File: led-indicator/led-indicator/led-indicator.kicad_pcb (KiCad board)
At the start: 2 copper layers, 49.9 x 35.7 mm, 36 parts, among them CN1 XT30U-M, J2 JST_XH_3pin, U1 74AHCT125

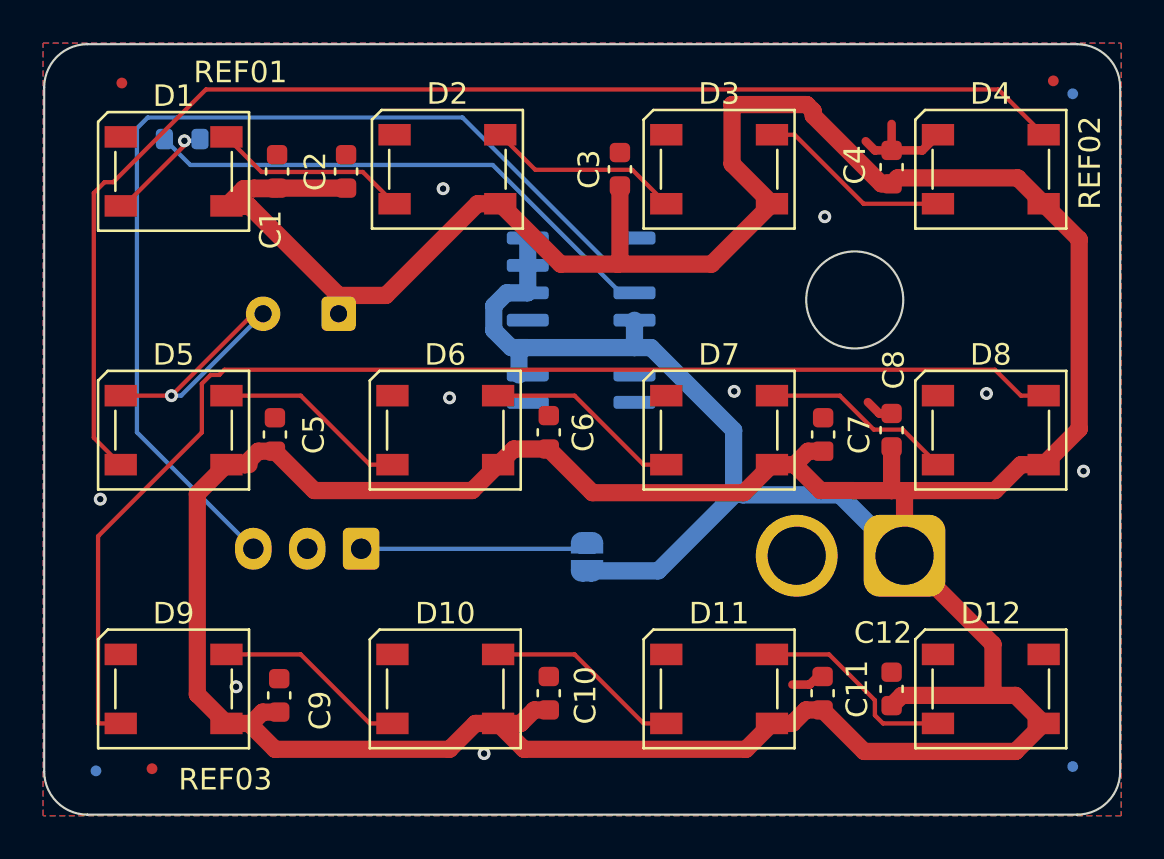
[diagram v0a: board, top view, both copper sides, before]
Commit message: Updated to be single-sided board.
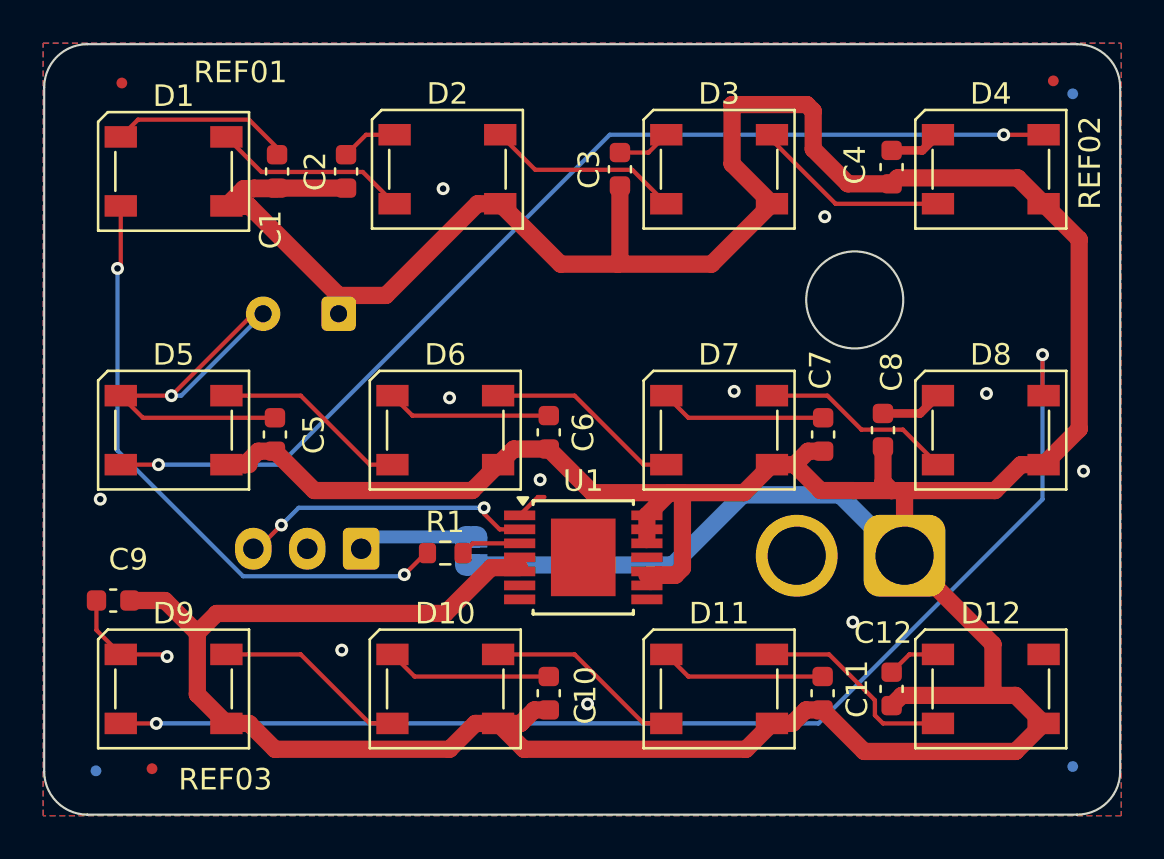
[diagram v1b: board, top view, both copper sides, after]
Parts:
- R1: moved to F.Cu
- U1: footprint Package_SO:SOIC-14_3.9x8.7mm_P1.27mm -> Package_SO:TSSOP-14-1EP_4.4x5mm_P0.65mm; moved to F.Cu
- moved R1 22.7 mm to (141.0, 108.5), turned to 0 degrees
- moved U1 11.0 mm to (147.4, 108.7), turned to 0 degrees
- moved C9 8.87 mm to (125.6, 110.7), turned to 180 degrees
- moved SJ1 5.38 mm to (142.2, 108.4)
- moved C8 0.40 mm to (161.3, 102.8)
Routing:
- net GND: track 21.5 -> 79.1 mm, vias 10 -> 13
- net /DIN: track 47.9 -> 13.5 mm, vias 0 -> 2
- net /DIN_5V: track 4.82 -> 28.6 mm, vias 1 -> 2
- net Net-(R1-Pad2): track 24.1 -> 2.81 mm
- net /D_4_5: track 60.0 -> 49.1 mm, vias 0 -> 2
- net Net-(J2-Pin_1): track 10.2 -> 4.55 mm
- net /D_8_9: track 58.6 -> 55.6 mm, vias 0 -> 2
- net +5V: track 243.9 -> 246.1 mm
